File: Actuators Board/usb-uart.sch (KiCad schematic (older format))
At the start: 11 parts

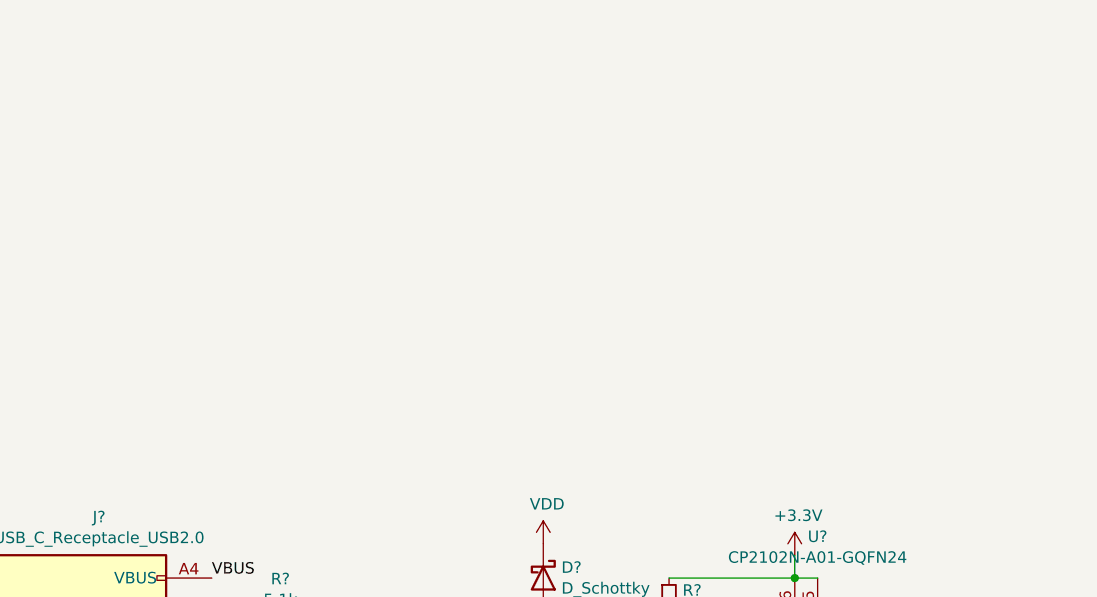
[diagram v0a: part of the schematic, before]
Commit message: CP2102 added and some connections
On the usb-uart board
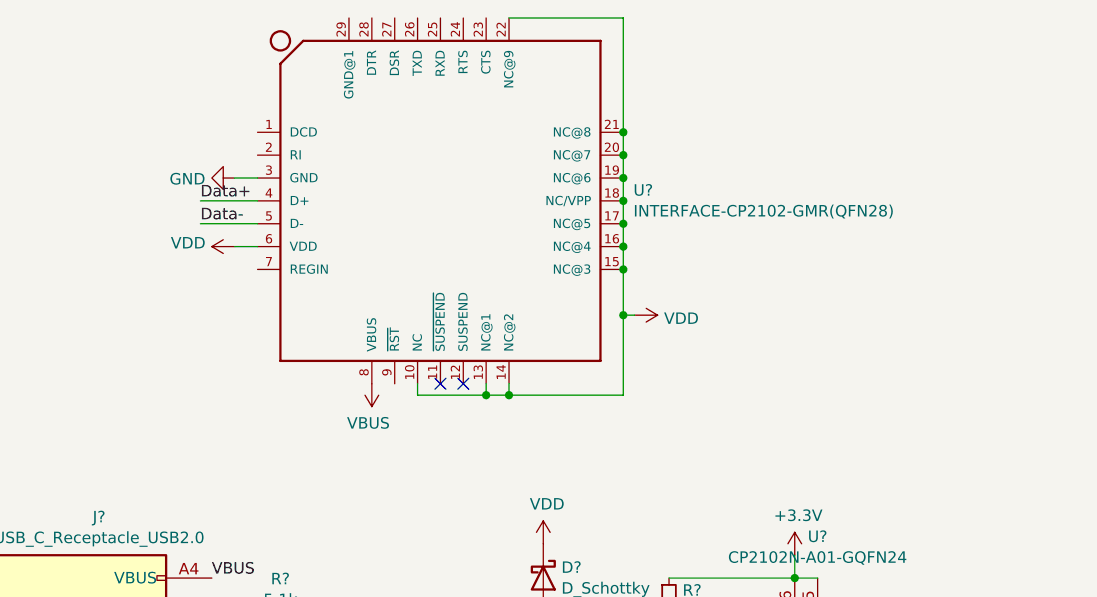
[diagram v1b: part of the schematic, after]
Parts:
- added U?: INTERFACE-CP2102-GMR(QFN28), QFN28G_0.5-5X5MM, symbol iclr:INTERFACE-CP2102-GMR(QFN28)
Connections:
- net Data+: now also U?.4 (D+)
- net Data-: now also U?.5 (D-)
- net GND: now also U?.3 (GND)
- net VBUS: now also U?.8 (VBUS)
- net VDD: now also U?.10 (NC), U?.13 (NC@1), U?.14 (NC@2), U?.15 (NC@3), U?.16 (NC@4), U?.17 (NC@5), U?.18 (NC/VPP), U?.19 (NC@6), U?.20 (NC@7), U?.21 (NC@8), U?.22 (NC@9), U?.6 (VDD)
- no-connect marks 12 -> 14
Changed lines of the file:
@@
 $Descr A4 11693 8268
 encoding utf-8
-Sheet 2 3
+Sheet 1 1
 Title ""
 Date ""
@@
 Wire Wire Line
 	4550 4250 4550 4300
+$Comp
+L iclr:INTERFACE-CP2102-GMR(QFN28) U?
+U 1 1 6198EFBF
+P 5550 1850
+F 0 "U?" H 6394 1896 50  0000 L CNN
+F 1 "INTERFACE-CP2102-GMR(QFN28)" H 6394 1805 50  0000 L CNN
+F 2 "QFN28G_0.5-5X5MM" H 5550 1850 50  0001 L BNN
+F 3 "" H 5550 1850 50  0001 L BNN
+F 4 "CP2102-GMR-QFN28" H 5550 1850 50  0001 L BNN "VALUE"
+F 5 "CP2102-GMR" H 5550 1850 50  0001 L BNN "MPN"
+	1    5550 1850
+	1    0    0    -1
+$EndComp
+$Comp
+L power:VDD #PWR?
+U 1 1 61993C98
+P 4650 2050
+F 0 "#PWR?" H 4650 1900 50  0001 C CNN
+F 1 "VDD" V 4665 2177 50  0000 L CNN
+F 2 "" H 4650 2050 50  0001 C CNN
+F 3 "" H 4650 2050 50  0001 C CNN
+	1    4650 2050
+	0    -1   -1   0
+$EndComp
+Wire Wire Line
+	4750 2050 4650 2050
+$Comp
+L power:GND #PWR?
+U 1 1 619952DA
+P 4650 1750
+F 0 "#PWR?" H 4650 1500 50  0001 C CNN
+F 1 "GND" V 4655 1622 50  0000 R CNN
+F 2 "" H 4650 1750 50  0001 C CNN
+F 3 "" H 4650 1750 50  0001 C CNN
+	1    4650 1750
+	0    1    1    0
+$EndComp
+Wire Wire Line
+	4650 1750 4750 1750
+$Comp
+L power:VBUS #PWR?
+U 1 1 61996CDA
+P 5250 2650
+F 0 "#PWR?" H 5250 2500 50  0001 C CNN
+F 1 "VBUS" H 5265 2823 50  0000 C CNN
+F 2 "" H 5250 2650 50  0001 C CNN
+F 3 "" H 5250 2650 50  0001 C CNN
+	1    5250 2650
+	-1   0    0    1
+$EndComp
+Text Label 4500 1950 0    50   ~ 0
+Data-
+Text Label 4500 1850 0    50   ~ 0
+Data+
+Wire Wire Line
+	4500 1850 4750 1850
+Wire Wire Line
+	4500 1950 4750 1950
+Wire Wire Line
+	6350 1550 6350 1650
+Wire Wire Line
+	6350 2700 5850 2700
+Wire Wire Line
+	5750 2700 5750 2650
+Connection ~ 6350 1650
+Wire Wire Line
+	6350 1650 6350 1750
+Connection ~ 6350 1750
+Wire Wire Line
+	6350 1750 6350 1850
+Connection ~ 6350 1850
+Wire Wire Line
+	6350 1850 6350 1950
+Connection ~ 6350 1950
+Wire Wire Line
+	6350 1950 6350 2050
+Connection ~ 6350 2050
+Wire Wire Line
+	6350 2050 6350 2150
+Connection ~ 6350 2150
+Wire Wire Line
+	6350 2150 6350 2350
+Wire Wire Line
+	5850 2650 5850 2700
+Connection ~ 5850 2700
+Wire Wire Line
+	5850 2700 5750 2700
+Wire Wire Line
+	6350 2350 6400 2350
+Connection ~ 6350 2350
+Wire Wire Line
+	6350 2350 6350 2700
+$Comp
+L power:VDD #PWR?
+U 1 1 6199D8ED
+P 6400 2350
+F 0 "#PWR?" H 6400 2200 50  0001 C CNN
+F 1 "VDD" V 6415 2478 50  0000 L CNN
+F 2 "" H 6400 2350 50  0001 C CNN
+F 3 "" H 6400 2350 50  0001 C CNN
+	1    6400 2350
+	0    1    1    0
+$EndComp
+Wire Wire Line
+	5450 2650 5450 2700
+Wire Wire Line
+	5450 2700 5750 2700
+Connection ~ 5750 2700
+Wire Wire Line
+	5850 1050 6350 1050
+Wire Wire Line
+	6350 1050 6350 1550
+Connection ~ 6350 1550
+NoConn ~ 5550 2650
+NoConn ~ 5650 2650
 $EndSCHEMATC

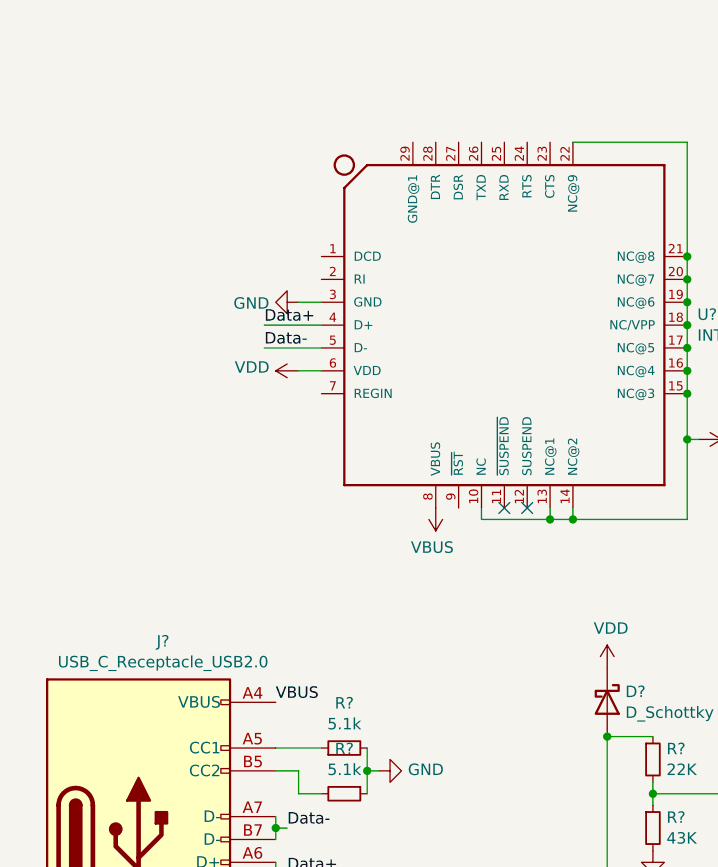
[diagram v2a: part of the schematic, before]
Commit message: Finished CP2102 connections
On Usb/Uart board
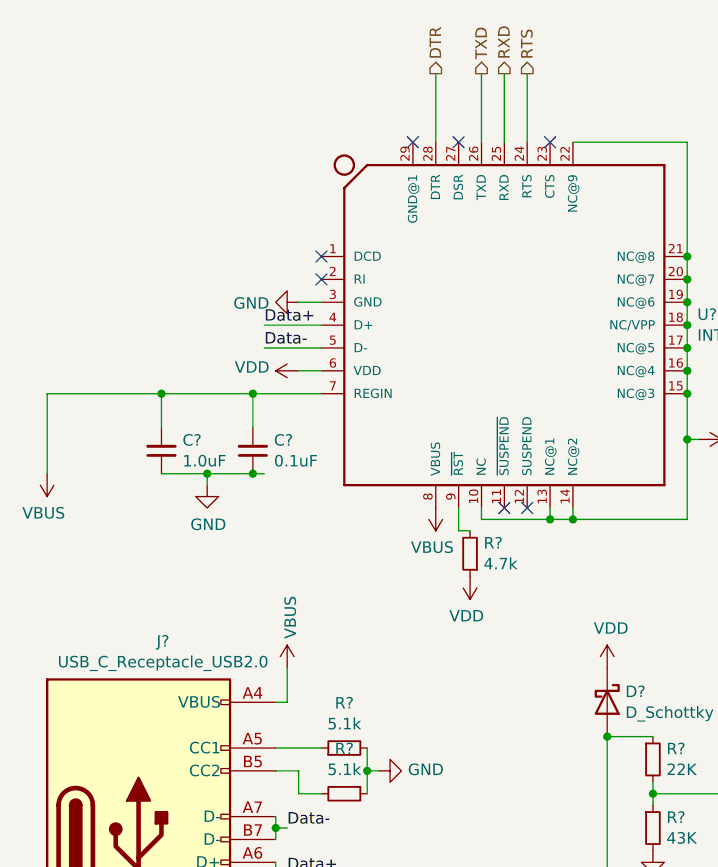
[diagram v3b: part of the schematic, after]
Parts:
- added C?: 1.0uF, symbol Device:C_Small
- added C?: 0.1uF, symbol Device:C_Small
- added R?: 4.7k, symbol Device:R_Small
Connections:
- net DTR: now also U?.28 (DTR)
- net GND: now also C?.1, C?.1
- net RTS: now also U?.24 (RTS)
- net RXD: now also U?.25 (RXD)
- net TXD: now also U?.26 (TXD)
- net VBUS: now also U?.7 (REGIN), C?.2, C?.2
- net VDD: now also R?.1
- net at U?.9 (~RST): now also R?.2
- no-connect marks 14 -> 19
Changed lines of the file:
@@
 $Descr A4 11693 8268
 encoding utf-8
-Sheet 1 3
+Sheet 1 1
 Title ""
 Date ""
@@
 Wire Wire Line
 	3650 5000 3800 5000
-Text Label 4550 3500 0    50   ~ 0
-VBUS
 Text Label 5800 4700 2    50   ~ 0
 VBUS
@@
 	4550 4250 4550 4300
 $Comp
+L power:VDD #PWR?
+U 1 1 61993C98
+P 4650 2050
+F 0 "#PWR?" H 4650 1900 50  0001 C CNN
+F 1 "VDD" V 4665 2177 50  0000 L CNN
+F 2 "" H 4650 2050 50  0001 C CNN
+F 3 "" H 4650 2050 50  0001 C CNN
+	1    4650 2050
+	0    -1   -1   0
+$EndComp
+$Comp
+L power:GND #PWR?
+U 1 1 619952DA
+P 4650 1750
+F 0 "#PWR?" H 4650 1500 50  0001 C CNN
+F 1 "GND" V 4655 1622 50  0000 R CNN
+F 2 "" H 4650 1750 50  0001 C CNN
+F 3 "" H 4650 1750 50  0001 C CNN
+	1    4650 1750
+	0    1    1    0
+$EndComp
+$Comp
+L power:VBUS #PWR?
+U 1 1 61996CDA
+P 5250 2650
+F 0 "#PWR?" H 5250 2500 50  0001 C CNN
+F 1 "VBUS" H 5265 2823 50  0000 C CNN
+F 2 "" H 5250 2650 50  0001 C CNN
+F 3 "" H 5250 2650 50  0001 C CNN
+	1    5250 2650
+	-1   0    0    1
+$EndComp
+Text Label 4500 1950 0    50   ~ 0
+Data-
+Text Label 4500 1850 0    50   ~ 0
+Data+
+Wire Wire Line
+	6350 2700 5850 2700
+Wire Wire Line
+	5750 2700 5750 2650
+Wire Wire Line
+	5850 2650 5850 2700
+Connection ~ 5850 2700
+Wire Wire Line
+	5850 2700 5750 2700
+Wire Wire Line
+	6350 2350 6400 2350
+Connection ~ 6350 2350
+Wire Wire Line
+	6350 2350 6350 2700
+$Comp
+L power:VDD #PWR?
+U 1 1 6199D8ED
+P 6400 2350
+F 0 "#PWR?" H 6400 2200 50  0001 C CNN
+F 1 "VDD" V 6415 2478 50  0000 L CNN
+F 2 "" H 6400 2350 50  0001 C CNN
+F 3 "" H 6400 2350 50  0001 C CNN
+	1    6400 2350
+	0    1    1    0
+$EndComp
+Wire Wire Line
+	5450 2650 5450 2700
+Wire Wire Line
+	5450 2700 5750 2700
+Connection ~ 5750 2700
+Wire Wire Line
+	5850 1050 6350 1050
+NoConn ~ 5550 2650
+NoConn ~ 5650 2650
+$Comp
+L power:VBUS #PWR?
+U 1 1 61A236C4
+P 4600 3350
+F 0 "#PWR?" H 4600 3200 50  0001 C CNN
+F 1 "VBUS" V 4615 3478 50  0000 L CNN
+F 2 "" H 4600 3350 50  0001 C CNN
+F 3 "" H 4600 3350 50  0001 C CNN
+	1    4600 3350
+	1    0    0    -1
+$EndComp
+Wire Wire Line
+	4600 3350 4600 3500
+Wire Wire Line
+	4600 3500 4550 3500
+Connection ~ 6350 1550
+Wire Wire Line
+	6350 1050 6350 1550
+Wire Wire Line
+	6350 2150 6350 2350
+Connection ~ 6350 2150
+Connection ~ 6350 2050
+Wire Wire Line
+	6350 2050 6350 2150
+Wire Wire Line
+	6350 1950 6350 2050
+Connection ~ 6350 1950
+Connection ~ 6350 1850
+Wire Wire Line
+	6350 1850 6350 1950
+Wire Wire Line
+	6350 1750 6350 1850
+Connection ~ 6350 1750
+Connection ~ 6350 1650
+Wire Wire Line
+	6350 1650 6350 1750
+Wire Wire Line
+	6350 1550 6350 1650
+Wire Wire Line
+	4750 2050 4650 2050
+Wire Wire Line
+	4500 1950 4750 1950
+Wire Wire Line
+	4500 1850 4750 1850
+Wire Wire Line
+	4650 1750 4750 1750
+$Comp
+L Device:C_Small C?
+U 1 1 61A2A124
+P 4450 2400
+F 0 "C?" H 4358 2354 50  0000 R CNN
+F 1 "0.1uF" H 4358 2445 50  0000 R CNN
+F 2 "" H 4450 2400 50  0001 C CNN
+F 3 "~" H 4450 2400 50  0001 C CNN
+	1    4450 2400
+	-1   0    0    1
+$EndComp
+$Comp
+L Device:C_Small C?
+U 1 1 61A28787
+P 4050 2400
+F 0 "C?" H 3958 2354 50  0000 R CNN
+F 1 "1.0uF" H 3958 2445 50  0000 R CNN
+F 2 "" H 4050 2400 50  0001 C CNN
+F 3 "~" H 4050 2400 50  0001 C CNN
+	1    4050 2400
+	-1   0    0    1
+$EndComp
+$Comp
 L iclr:INTERFACE-CP2102-GMR(QFN28) U?
 U 1 1 6198EFBF
@@
 	1    0    0    -1
 $EndComp
+Wire Wire Line
+	3550 2150 3550 2500
+Wire Wire Line
+	4050 2300 4050 2150
+Connection ~ 4050 2150
+Wire Wire Line
+	4050 2150 3550 2150
+Wire Wire Line
+	4450 2300 4450 2150
+Wire Wire Line
+	4050 2500 4250 2500
+$Comp
+L power:GND #PWR?
+U 1 1 61A3A0E4
+P 4250 2550
+F 0 "#PWR?" H 4250 2300 50  0001 C CNN
+F 1 "GND" H 4255 2377 50  0000 C CNN
+F 2 "" H 4250 2550 50  0001 C CNN
+F 3 "" H 4250 2550 50  0001 C CNN
+	1    4250 2550
+	1    0    0    -1
+$EndComp
+Wire Wire Line
+	4250 2500 4250 2550
+Connection ~ 4250 2500
+Wire Wire Line
+	4250 2500 4450 2500
+Wire Wire Line
+	4050 2150 4450 2150
+Wire Wire Line
+	4450 2500 4500 2500
+Connection ~ 4450 2500
+Connection ~ 4450 2150
+Wire Wire Line
+	4450 2150 4750 2150
+$Comp
+L power:VBUS #PWR?
+U 1 1 61A46D5F
+P 3550 2500
+F 0 "#PWR?" H 3550 2350 50  0001 C CNN
+F 1 "VBUS" H 3565 2673 50  0000 C CNN
+F 2 "" H 3550 2500 50  0001 C CNN
+F 3 "" H 3550 2500 50  0001 C CNN
+	1    3550 2500
+	-1   0    0    1
+$EndComp
+Wire Wire Line
+	5650 1050 5650 750
+Text HLabel 5650 750  1    50   Output ~ 0
+RTS
+Wire Wire Line
+	5550 1050 5550 750
+Text HLabel 5550 750  1    50   Output ~ 0
+RXD
+Wire Wire Line
+	5250 1050 5250 750
+Text HLabel 5250 750  1    50   Output ~ 0
+DTR
+Wire Wire Line
+	5450 1050 5450 750
+Text HLabel 5450 750  1    50   Output ~ 0
+TXD
+NoConn ~ 5350 1050
+NoConn ~ 4750 1550
+NoConn ~ 4750 1650
+NoConn ~ 5750 1050
+NoConn ~ 5150 1050
+$Comp
+L Device:R_Small R?
+U 1 1 61A58884
+P 5400 2850
+F 0 "R?" H 5341 2804 50  0000 R CNN
+F 1 "4.7k" H 5341 2895 50  0000 R CNN
+F 2 "" H 5400 2850 50  0001 C CNN
+F 3 "~" H 5400 2850 50  0001 C CNN
+	1    5400 2850
+	-1   0    0    1
+$EndComp
+Wire Wire Line
+	5350 2650 5350 2750
+Wire Wire Line
+	5350 2750 5400 2750
 $Comp
 L power:VDD #PWR?
-U 1 1 61993C98
-P 4650 2050
-F 0 "#PWR?" H 4650 1900 50  0001 C CNN
-F 1 "VDD" V 4665 2177 50  0000 L CNN
-F 2 "" H 4650 2050 50  0001 C CNN
-F 3 "" H 4650 2050 50  0001 C CNN
-	1    4650 2050
-	0    -1   -1   0
-$EndComp
-Wire Wire Line
-	4750 2050 4650 2050
-$Comp
-L power:GND #PWR?
-U 1 1 619952DA
-P 4650 1750
-F 0 "#PWR?" H 4650 1500 50  0001 C CNN
-F 1 "GND" V 4655 1622 50  0000 R CNN
-F 2 "" H 4650 1750 50  0001 C CNN
-F 3 "" H 4650 1750 50  0001 C CNN
-	1    4650 1750
-	0    1    1    0
-$EndComp
-Wire Wire Line
-	4650 1750 4750 1750
-$Comp
-L power:VBUS #PWR?
-U 1 1 61996CDA
-P 5250 2650
-F 0 "#PWR?" H 5250 2500 50  0001 C CNN
-F 1 "VBUS" H 5265 2823 50  0000 C CNN
-F 2 "" H 5250 2650 50  0001 C CNN
-F 3 "" H 5250 2650 50  0001 C CNN
-	1    5250 2650
+U 1 1 61A5BB13
+P 5400 2950
+F 0 "#PWR?" H 5400 2800 50  0001 C CNN
+F 1 "VDD" H 5415 3123 50  0000 C CNN
+F 2 "" H 5400 2950 50  0001 C CNN
+F 3 "" H 5400 2950 50  0001 C CNN
+	1    5400 2950
 	-1   0    0    1
 $EndComp
-Text Label 4500 1950 0    50   ~ 0
-Data-
-Text Label 4500 1850 0    50   ~ 0
-Data+
-Wire Wire Line
-	4500 1850 4750 1850
-Wire Wire Line
-	4500 1950 4750 1950
-Wire Wire Line
-	6350 1550 6350 1650
-Wire Wire Line
-	6350 2700 5850 2700
-Wire Wire Line
-	5750 2700 5750 2650
-Connection ~ 6350 1650
-Wire Wire Line
-	6350 1650 6350 1750
-Connection ~ 6350 1750
-Wire Wire Line
-	6350 1750 6350 1850
-Connection ~ 6350 1850
-Wire Wire Line
-	6350 1850 6350 1950
-Connection ~ 6350 1950
-Wire Wire Line
-	6350 1950 6350 2050
-Connection ~ 6350 2050
-Wire Wire Line
-	6350 2050 6350 2150
-Connection ~ 6350 2150
-Wire Wire Line
-	6350 2150 6350 2350
-Wire Wire Line
-	5850 2650 5850 2700
-Connection ~ 5850 2700
-Wire Wire Line
-	5850 2700 5750 2700
-Wire Wire Line
-	6350 2350 6400 2350
-Connection ~ 6350 2350
-Wire Wire Line
-	6350 2350 6350 2700
-$Comp
-L power:VDD #PWR?
-U 1 1 6199D8ED
-P 6400 2350
-F 0 "#PWR?" H 6400 2200 50  0001 C CNN
-F 1 "VDD" V 6415 2478 50  0000 L CNN
-F 2 "" H 6400 2350 50  0001 C CNN
-F 3 "" H 6400 2350 50  0001 C CNN
-	1    6400 2350
-	0    1    1    0
-$EndComp
-Wire Wire Line
-	5450 2650 5450 2700
-Wire Wire Line
-	5450 2700 5750 2700
-Connection ~ 5750 2700
-Wire Wire Line
-	5850 1050 6350 1050
-Wire Wire Line
-	6350 1050 6350 1550
-Connection ~ 6350 1550
-NoConn ~ 5550 2650
-NoConn ~ 5650 2650
 $EndSCHEMATC
